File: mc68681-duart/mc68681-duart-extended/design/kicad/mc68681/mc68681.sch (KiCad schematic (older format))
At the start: 31 parts, among them IC1 XR68C681CJTR-F, IC2 74HCT245, IC3 74HCT245, IC4 74HCT245, IC5 74125, IC6 IC6_DECO.PLD, IC7 IC7_UART_.PLD, J1 Conn_02x32_Odd_Even, J2 EXTBUS, J3 UART_A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

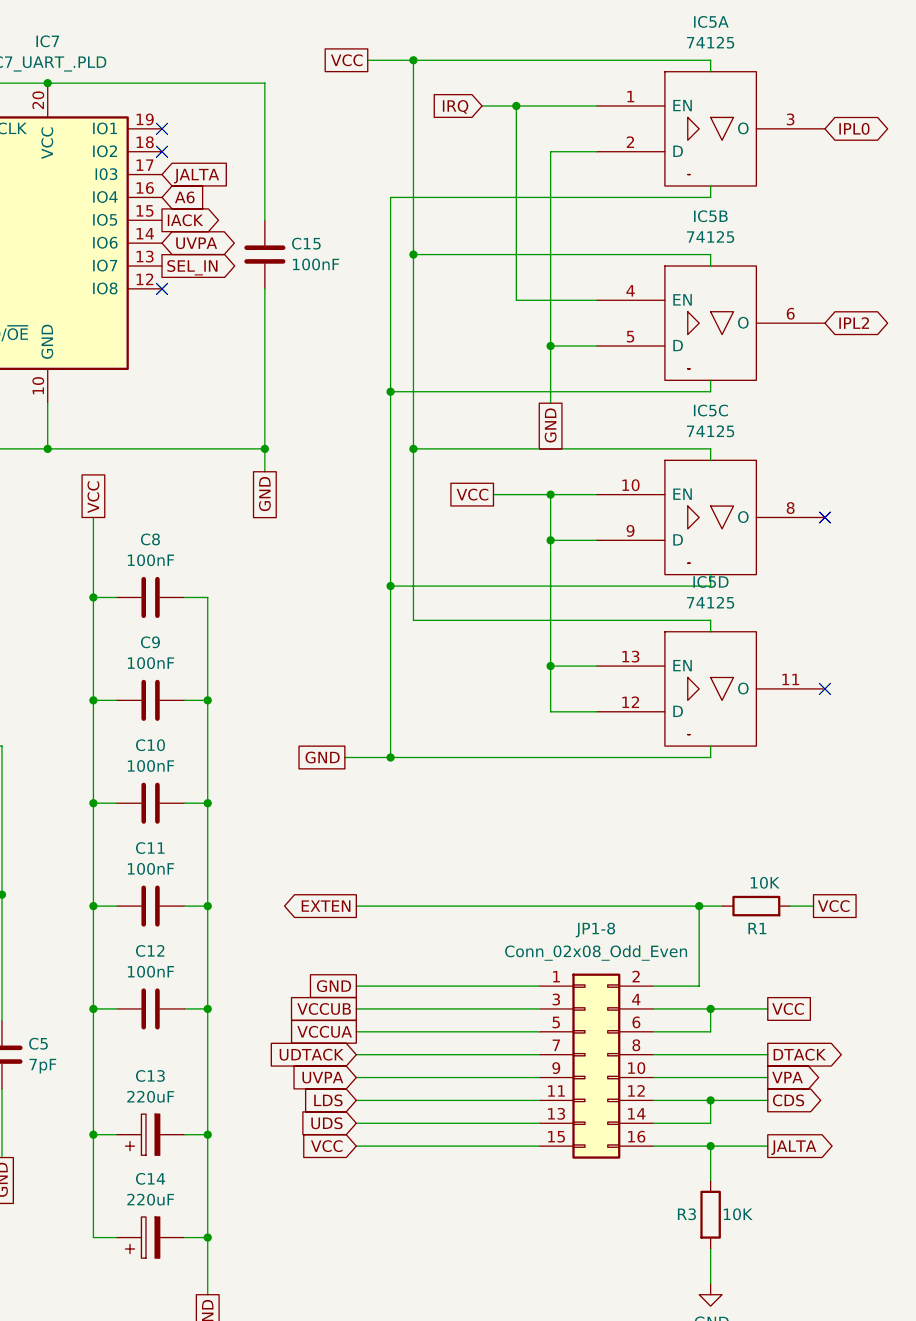
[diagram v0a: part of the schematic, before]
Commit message: Glue updated and silkscreen fixed
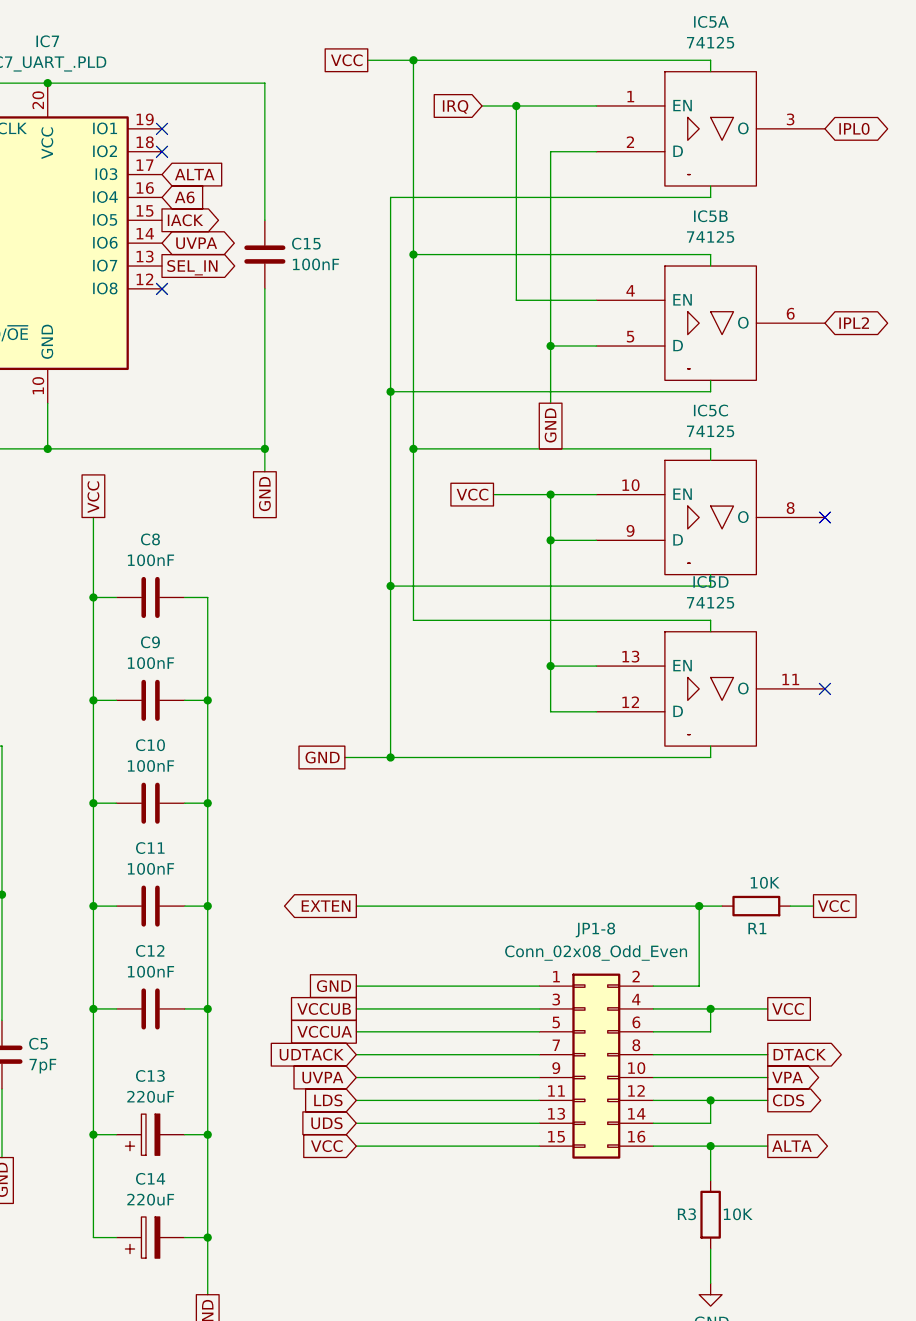
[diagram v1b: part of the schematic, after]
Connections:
- net JALTA renamed ALTA
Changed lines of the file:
@@
 A6
 Text GLabel 7900 1300 2    50   Input ~ 0
-JALTA
+ALTA
 Wire Wire Line
 	9550 5550 8750 5550
@@
 VCC
 Text GLabel 10550 5550 2    50   Output ~ 0
-JALTA
+ALTA
 $Comp
 L Device:R R3

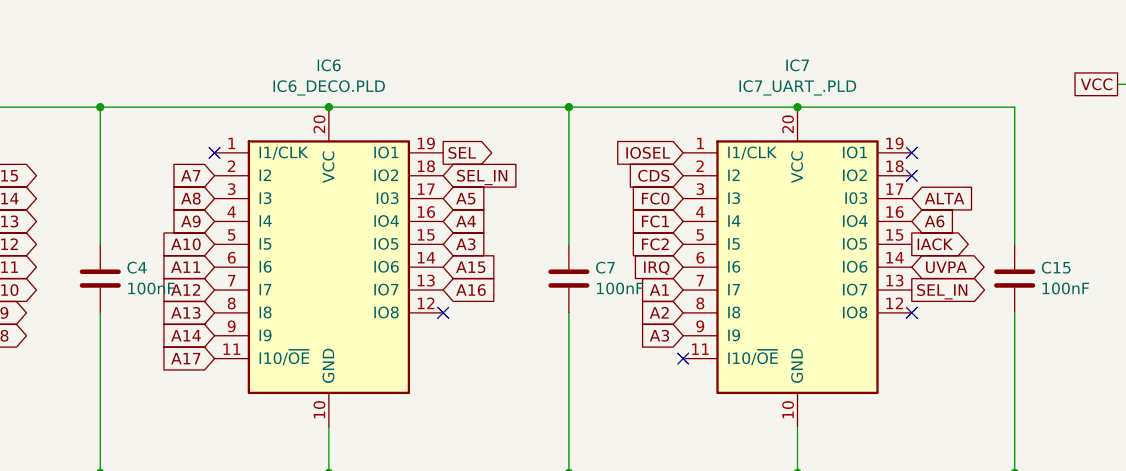
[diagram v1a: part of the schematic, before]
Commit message: Update for new r2 base address
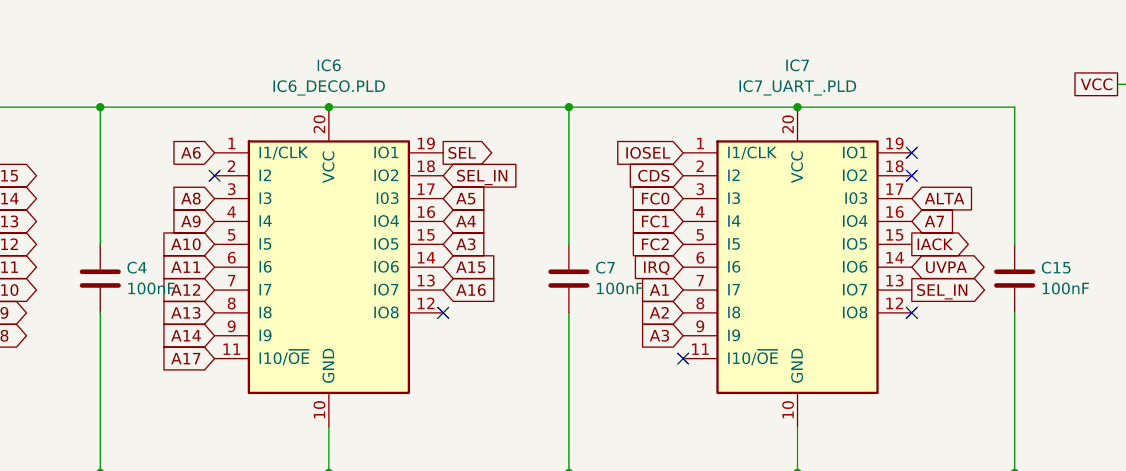
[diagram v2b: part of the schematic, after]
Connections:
- net A6: now also IC6.1 (I1/CLK); no longer IC7.16 (IO4)
- net A7: now also IC7.16 (IO4); no longer IC6.2 (I2)
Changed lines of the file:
@@
 	1    0    0    -1
 $EndComp
-Text GLabel 4850 1200 0    50   Input ~ 0
-A7
 Text GLabel 4850 1300 0    50   Input ~ 0
 A8
@@
 NoConn ~ 5850 1800
 Text GLabel 7900 1400 2    50   Input ~ 0
-A6
+A7
 Text GLabel 7900 1300 2    50   Input ~ 0
 ALTA
@@
 Wire Wire Line
 	10300 6000 10300 6150
-NoConn ~ 4850 1100
+NoConn ~ 4850 1200
 Wire Wire Line
 	8750 5350 9550 5350
 Text GLabel 1050 2200 0    50   Output ~ 0
 LDS
+Text GLabel 4850 1100 0    50   Input ~ 0
+A6
 $EndSCHEMATC
